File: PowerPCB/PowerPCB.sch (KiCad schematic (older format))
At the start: 22 parts, among them J1 Conn_01x03_Male, J2 Conn_01x08_Male, J3 STM Inputs, J4 STM Outputs, J5 Conn_01x07_Male, K1 HF3-06, U1 NCP1117-3.3_SOT223, U2 STM32F413ZHTx

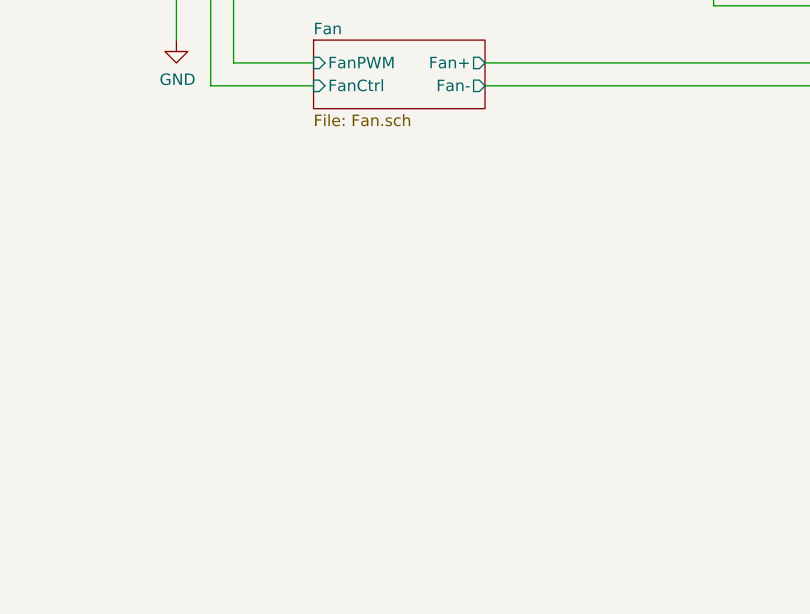
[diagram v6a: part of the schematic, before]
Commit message: Added 3A SPST relays for all relays
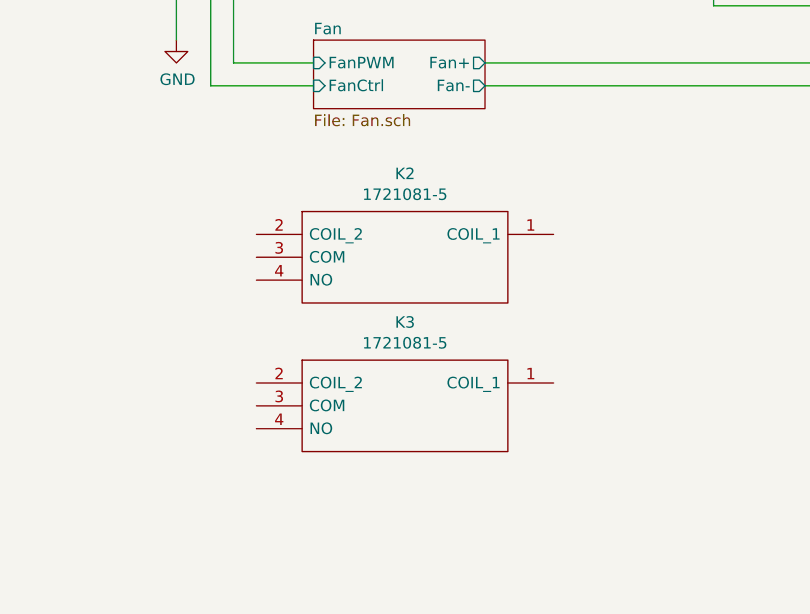
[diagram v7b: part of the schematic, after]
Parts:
- added K2, K3: 1721081-5, SamacSys_Parts:17210815, symbol SamacSys_Parts:1721081-5
- J1: footprint Connector_PinHeader_1.00mm:PinHeader_1x03_P1.00mm_Vertical -> Connector_PinHeader_2.54mm:PinHeader_1x03_P2.54mm_Horizontal
- J2: footprint Connector_PinHeader_1.00mm:PinHeader_1x08_P1.00mm_Vertical -> Connector_PinHeader_2.54mm:PinHeader_1x08_P2.54mm_Horizontal
- J3, J4, J5: footprint Connector_PinHeader_1.00mm:PinHeader_1x07_P1.00mm_Vertical -> Connector_PinHeader_2.54mm:PinHeader_1x07_P2.54mm_Horizontal
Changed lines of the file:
@@
 F 0 "J4" H 6308 2331 50  0000 C CNN
 F 1 "STM Outputs" H 6308 2240 50  0000 C CNN
-F 2 "Connector_PinHeader_1.00mm:PinHeader_1x07_P1.00mm_Vertical" H 6200 1850 50  0001 C CNN
+F 2 "Connector_PinHeader_2.54mm:PinHeader_1x07_P2.54mm_Horizontal" H 6200 1850 50  0001 C CNN
 F 3 "~" H 6200 1850 50  0001 C CNN
 	1    6200 1850
@@
 F 0 "J5" H 8100 4000 50  0000 R CNN
 F 1 "Conn_01x07_Male" H 8200 3900 50  0000 R CNN
-F 2 "Connector_PinHeader_1.00mm:PinHeader_1x07_P1.00mm_Vertical" H 8150 3500 50  0001 C CNN
+F 2 "Connector_PinHeader_2.54mm:PinHeader_1x07_P2.54mm_Horizontal" H 8150 3500 50  0001 C CNN
 F 3 "~" H 8150 3500 50  0001 C CNN
 	1    8150 3500
@@
 F 0 "J3" H 5150 2450 50  0000 R CNN
 F 1 "STM Inputs" H 5300 2350 50  0000 R CNN
-F 2 "Connector_PinHeader_1.00mm:PinHeader_1x07_P1.00mm_Vertical" H 5200 1850 50  0001 C CNN
+F 2 "Connector_PinHeader_2.54mm:PinHeader_1x07_P2.54mm_Horizontal" H 5200 1850 50  0001 C CNN
 F 3 "~" H 5200 1850 50  0001 C CNN
 	1    5200 1850
@@
 F 0 "J2" H 1450 3000 50  0000 C CNN
 F 1 "Conn_01x08_Male" H 1400 2900 50  0000 C CNN
-F 2 "Connector_PinHeader_1.00mm:PinHeader_1x08_P1.00mm_Vertical" H 1300 2450 50  0001 C CNN
+F 2 "Connector_PinHeader_2.54mm:PinHeader_1x08_P2.54mm_Horizontal" H 1300 2450 50  0001 C CNN
 F 3 "~" H 1300 2450 50  0001 C CNN
 	1    1300 2450
@@
 F 0 "J1" H 1408 1831 50  0000 C CNN
 F 1 "Conn_01x03_Male" H 1408 1740 50  0000 C CNN
-F 2 "Connector_PinHeader_1.00mm:PinHeader_1x03_P1.00mm_Vertical" H 1300 1550 50  0001 C CNN
+F 2 "Connector_PinHeader_2.54mm:PinHeader_1x03_P2.54mm_Horizontal" H 1300 1550 50  0001 C CNN
 F 3 "~" H 1300 1550 50  0001 C CNN
 	1    1300 1550
@@
 	1    0    0    -1
 $EndComp
+$Comp
+L SamacSys_Parts:1721081-5 K2
+U 1 1 5ED2417F
+P 2050 4300
+F 0 "K2" H 2700 4565 50  0000 C CNN
+F 1 "1721081-5" H 2700 4474 50  0000 C CNN
+F 2 "SamacSys_Parts:17210815" H 3200 4400 50  0001 L CNN
+F 3 "https://www.te.com/commerce/DocumentDelivery/DDEController?Action=showdoc&DocId=Customer+Drawing%7F1721081%7FD1%7Fpdf%7FEnglish%7FENG_CD_1721081_D1.pdf%7F1721081-5" H 3200 4300 50  0001 L CNN
+F 4 "SPDT-NO PCB Mount Latching Relay Through Hole, 3 A, 12V dc" H 3200 4200 50  0001 L CNN "Description"
+F 5 "15" H 3200 4100 50  0001 L CNN "Height"
+F 6 "655-1721081-5" H 3200 4000 50  0001 L CNN "Mouser Part Number"
+F 7 "https://www.mouser.co.uk/ProductDetail/TE-Connectivity-OEG/1721081-5?qs=BqFpTYCQ3dI5UJqEVQS1jg%3D%3D" H 3200 3900 50  0001 L CNN "Mouser Price/Stock"
+F 8 "TE Connectivity" H 3200 3800 50  0001 L CNN "Manufacturer_Name"
+F 9 "1721081-5" H 3200 3700 50  0001 L CNN "Manufacturer_Part_Number"
+	1    2050 4300
+	1    0    0    -1
+$EndComp
+$Comp
+L SamacSys_Parts:1721081-5 K3
+U 1 1 5ED25C0D
+P 2050 4950
+F 0 "K3" H 2700 5215 50  0000 C CNN
+F 1 "1721081-5" H 2700 5124 50  0000 C CNN
+F 2 "SamacSys_Parts:17210815" H 3200 5050 50  0001 L CNN
+F 3 "https://www.te.com/commerce/DocumentDelivery/DDEController?Action=showdoc&DocId=Customer+Drawing%7F1721081%7FD1%7Fpdf%7FEnglish%7FENG_CD_1721081_D1.pdf%7F1721081-5" H 3200 4950 50  0001 L CNN
+F 4 "SPDT-NO PCB Mount Latching Relay Through Hole, 3 A, 12V dc" H 3200 4850 50  0001 L CNN "Description"
+F 5 "15" H 3200 4750 50  0001 L CNN "Height"
+F 6 "655-1721081-5" H 3200 4650 50  0001 L CNN "Mouser Part Number"
+F 7 "https://www.mouser.co.uk/ProductDetail/TE-Connectivity-OEG/1721081-5?qs=BqFpTYCQ3dI5UJqEVQS1jg%3D%3D" H 3200 4550 50  0001 L CNN "Mouser Price/Stock"
+F 8 "TE Connectivity" H 3200 4450 50  0001 L CNN "Manufacturer_Name"
+F 9 "1721081-5" H 3200 4350 50  0001 L CNN "Manufacturer_Part_Number"
+	1    2050 4950
+	1    0    0    -1
+$EndComp

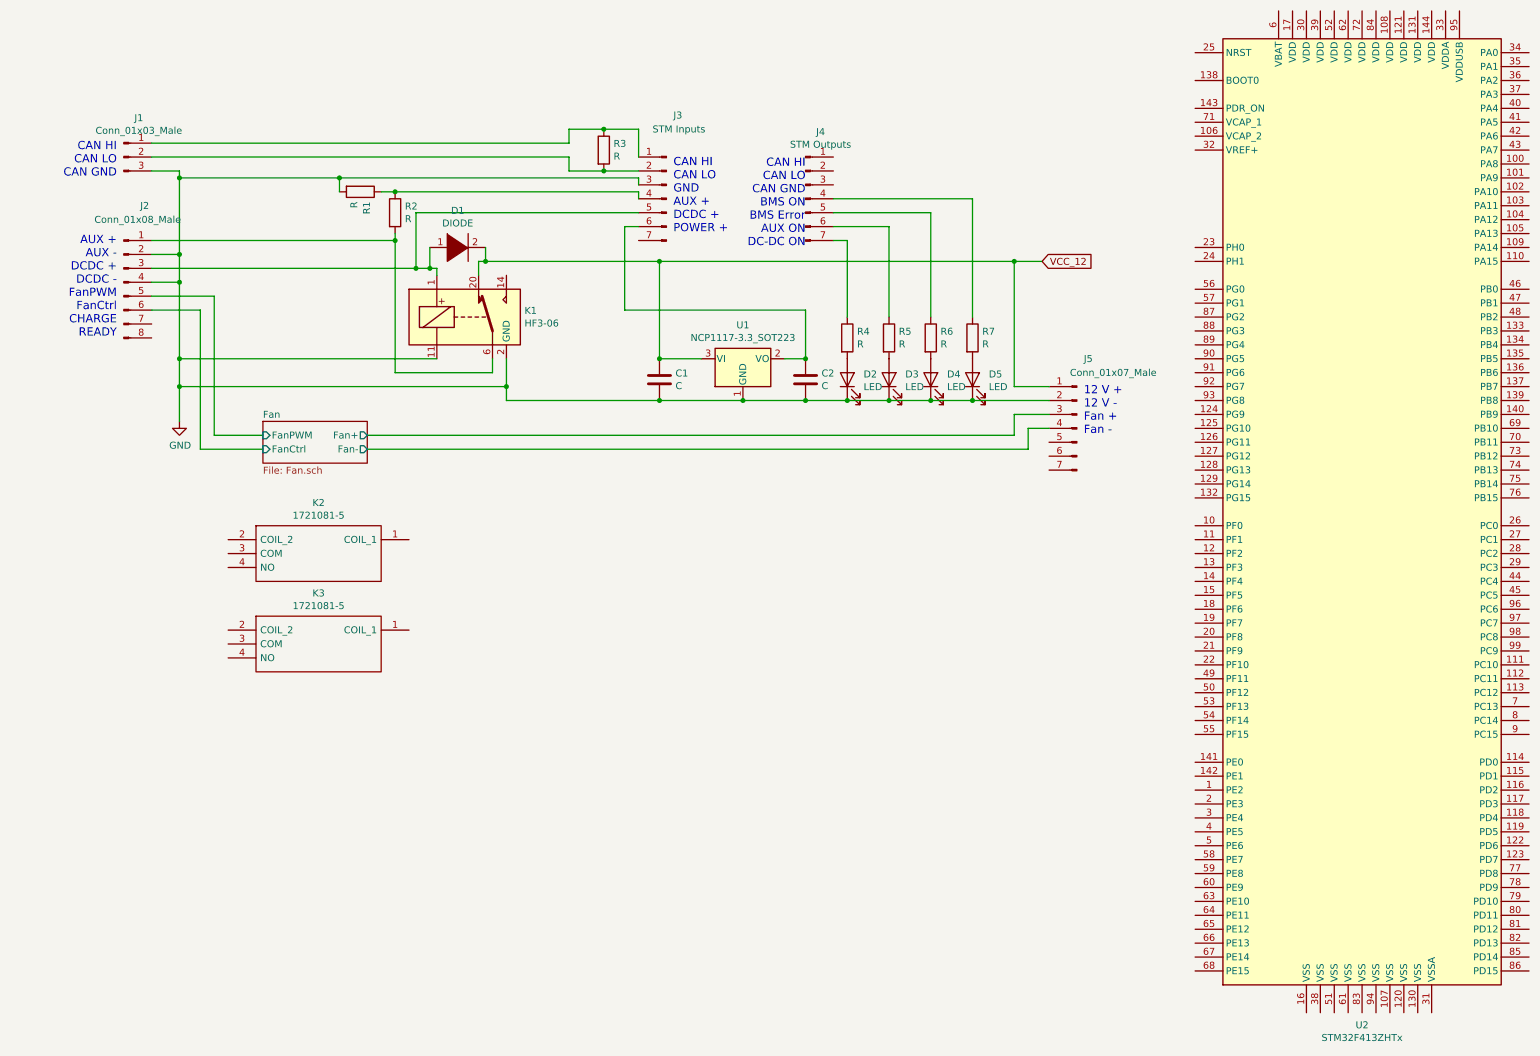
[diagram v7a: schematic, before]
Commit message: Removed SPDT chassis mount relay, added diode footprint
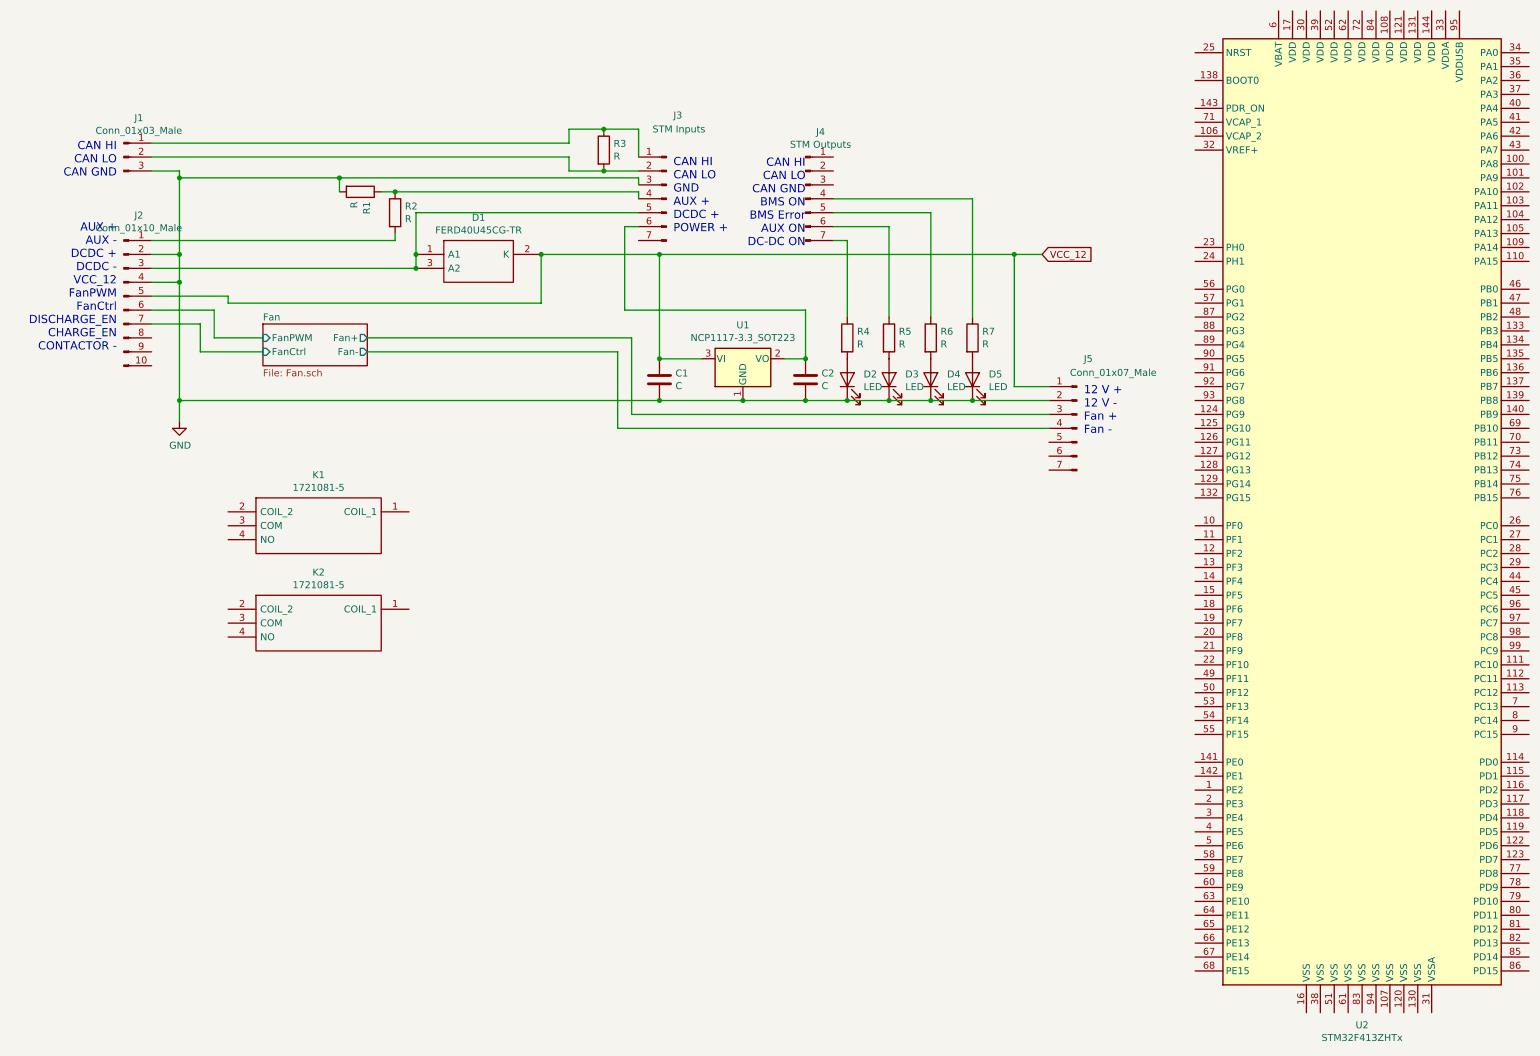
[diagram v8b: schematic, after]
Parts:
- removed D1: DIODE, Diode_SMD:D_0805_2012Metric_Pad1.15x1.40mm_HandSolder, symbol pspice:DIODE
- removed J2: Conn_01x08_Male, Connector_PinHeader_2.54mm:PinHeader_1x08_P2.54mm_Horizontal, symbol Connector:Conn_01x08_Male
- removed K1: HF3-06, Relay_SMD:Relay_SPDT_AXICOM_HF3Series_75ohms_Pitch1.27mm, symbol Relay:HF3-06
- removed K3: 1721081-5, SamacSys_Parts:17210815, symbol SamacSys_Parts:1721081-5
- added D1: FERD40U45CG-TR, SamacSys_Parts:FERD40U45CGTR, symbol SamacSys_Parts:FERD40U45CG-TR
- added J2: Conn_01x10_Male, Connector_PinHeader_2.54mm:PinHeader_1x10_P2.54mm_Horizontal, symbol Connector:Conn_01x10_Male
- added K1: 1721081-5, SamacSys_Parts:17210815, symbol SamacSys_Parts:1721081-5
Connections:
- net Fan/FanCtrl: now also J2.7 (Pin_7)
- net Fan/FanPWM: now also J2.6 (Pin_6)
- net GND: now also J2.2 (Pin_2), J2.4 (Pin_4)
- net VCC_12: now also D1.2 (K), J2.5 (Pin_5)
- net at R2.2: now also J2.1 (Pin_1)
- net at J3.5 (Pin_5): now also D1.1 (A1), D1.3 (A2), J2.3 (Pin_3)
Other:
- note added: "AUX +\nAUX -\nDCDC +\nDCDC -\nVCC_12\nFanPWM\nFanCtrl\nDISCHARGE_EN\nCHARGE_EN\nCONTACTOR -"
- note removed: "AUX +\nAUX -\nDCDC +\nDCDC -\nFanPWM\nFanCtrl\nCHARGE\nREADY"
